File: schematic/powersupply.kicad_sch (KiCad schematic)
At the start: 15 parts

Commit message: Update schematic
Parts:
- added D13: 1N5908, Diode_THT:D_DO-201AE_P15.24mm_Horizontal, symbol Diode:1N5908
- C10: value 680 nF / 400 V -> 680 nF / 400 V= 250 V~
- C9: value 220 nF / 400 V -> 220 nF / 400 V= 250 V~
- R10, R11: value 100 / 0.5 W -> 100 / 2 W
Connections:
- net +5V: now also D13.1 (A1)
- net GND: now also D13.2 (A2)
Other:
- note added: "TVS"
- moved on the sheet: C10, C9, R10, R11, R12, R13, R14, R15

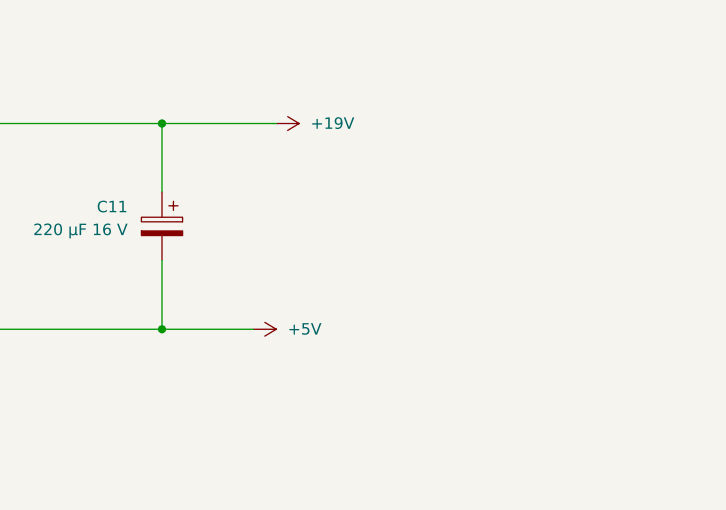
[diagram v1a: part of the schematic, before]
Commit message: schematic: Add TVS
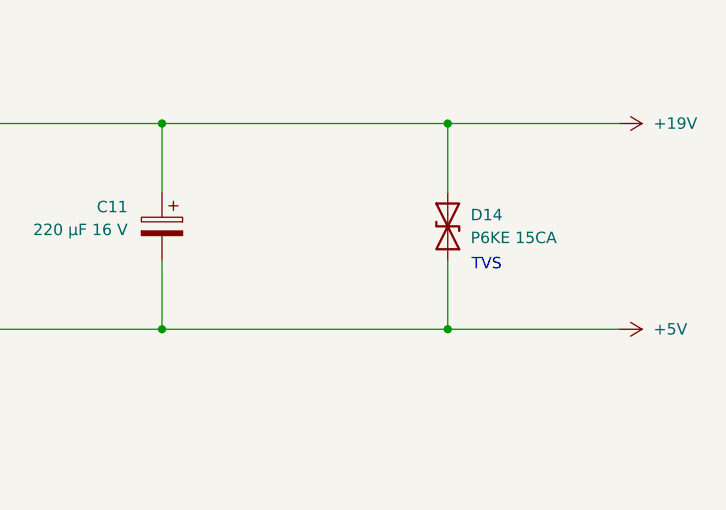
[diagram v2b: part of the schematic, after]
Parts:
- added D14: P6KE 15CA, Diode_THT:D_DO-201AE_P15.24mm_Horizontal, symbol Diode:1N62xxCA
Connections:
- net +19V: now also D14.2 (A2)
- net +5V: now also D14.1 (A1)
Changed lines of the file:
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@@
 		(company "Michael Büsch <m@bues.ch>")
+	)
+	(text "TVS"
+		(exclude_from_sim no)
+		(at 210.058 66.548 0)
+		(effects
+			(font
+				(size 1.27 1.27)
+			)
+		)
 	)
 	(text "+19 V rail"
@@
 	)
 	(junction
+		(at 205.74 50.8)
+		(diameter 0)
+		(color 0 0 0 0)
+	)
+	(junction
 		(at 180.34 115.57)
+		(diameter 0)
+		(color 0 0 0 0)
+	)
+	(junction
+		(at 205.74 73.66)
 		(diameter 0)
 		(color 0 0 0 0)
@@
 	(wire
 		(pts
+			(xy 205.74 66.04) (xy 205.74 73.66)
+		)
+		(stroke
+			(width 0)
+			(type default)
+		)
+	)
+	(wire
+		(pts
 			(xy 118.11 125.73) (xy 124.46 125.73)
 		)
@@
 	(wire
 		(pts
+			(xy 205.74 50.8) (xy 205.74 58.42)
+		)
+		(stroke
+			(width 0)
+			(type default)
+		)
+	)
+	(wire
+		(pts
 			(xy 147.32 71.12) (xy 147.32 73.66)
 		)
@@
 	(wire
 		(pts
-			(xy 173.99 73.66) (xy 184.15 73.66)
+			(xy 205.74 50.8) (xy 224.79 50.8)
+		)
+		(stroke
+			(width 0)
+			(type default)
+		)
+	)
+	(wire
+		(pts
+			(xy 173.99 73.66) (xy 205.74 73.66)
 		)
 		(stroke
@@
 	(wire
 		(pts
-			(xy 173.99 50.8) (xy 186.69 50.8)
+			(xy 173.99 50.8) (xy 205.74 50.8)
 		)
 		(stroke
@@
 		(pts
 			(xy 173.99 66.04) (xy 173.99 73.66)
+		)
+		(stroke
+			(width 0)
+			(type default)
+		)
+	)
+	(wire
+		(pts
+			(xy 205.74 73.66) (xy 224.79 73.66)
 		)
 		(stroke
@@
 	(symbol
 		(lib_id "power:+15V")
-		(at 186.69 50.8 270)
+		(at 224.79 50.8 270)
 		(unit 1)
 		(exclude_from_sim no)
@@
 		(fields_autoplaced yes)
 		(property "Reference" "#PWR016"
-			(at 182.88 50.8 0)
+			(at 220.98 50.8 0)
 			(effects
 				(font
@@
 		)
 		(property "Value" "+19V"
-			(at 190.5 50.7999 90)
+			(at 228.6 50.7999 90)
 			(effects
 				(font
@@
 		)
 		(property "Footprint" ""
-			(at 186.69 50.8 0)
+			(at 224.79 50.8 0)
 			(effects
 				(font
@@
 		)
 		(property "Datasheet" ""
-			(at 186.69 50.8 0)
+			(at 224.79 50.8 0)
 			(effects
 				(font
@@
 		)
 		(property "Description" "Power symbol creates a global label with name \"+15V\""
-			(at 186.69 50.8 0)
+			(at 224.79 50.8 0)
 			(effects
 				(font
@@
 	)
 	(symbol
+		(lib_id "Diode:1N62xxCA")
+		(at 205.74 62.23 90)
+		(unit 1)
+		(exclude_from_sim no)
+		(in_bom yes)
+		(on_board yes)
+		(dnp no)
+		(fields_autoplaced yes)
+		(property "Reference" "D14"
+			(at 208.28 60.9599 90)
+			(effects
+				(font
+					(size 1.27 1.27)
+				)
+				(justify right)
+			)
+		)
+		(property "Value" "P6KE 15CA"
+			(at 208.28 63.4999 90)
+			(effects
+				(font
+					(size 1.27 1.27)
+				)
+				(justify right)
+			)
+		)
+		(property "Footprint" "Diode_THT:D_DO-201AE_P15.24mm_Horizontal"
+			(at 210.82 62.23 0)
+			(effects
+				(font
+					(size 1.27 1.27)
+				)
+				(hide yes)
+			)
+		)
+		(property "Datasheet" "https://www.vishay.com/docs/88301/15ke.pdf"
+			(at 205.74 62.23 0)
+			(effects
+				(font
+					(size 1.27 1.27)
+				)
+				(hide yes)
+			)
+		)
+		(property "Description" "1500W bidirectional TRANSZORB® Transient Voltage Suppressor, DO-201AE"
+			(at 205.74 62.23 0)
+			(effects
+				(font
+					(size 1.27 1.27)
+				)
+				(hide yes)
+			)
+		)
+		(pin "1"
+		)
+		(pin "2"
+		)
+		(instances
+			(project "phaseanglecontrol"
+				(path "/167e0419-9f88-4ea4-ae96-d03af9cd26b8/bb8c6d96-af7e-4cb3-a868-b4a7ef100530"
+					(reference "D14")
+					(unit 1)
+				)
+			)
+		)
+	)
+	(symbol
 		(lib_id "Device:C_Polarized")
 		(at 173.99 125.73 0)
@@
 	(symbol
 		(lib_id "power:+5V")
-		(at 184.15 73.66 270)
+		(at 224.79 73.66 270)
 		(unit 1)
 		(exclude_from_sim no)
@@
 		(fields_autoplaced yes)
 		(property "Reference" "#PWR013"
-			(at 180.34 73.66 0)
+			(at 220.98 73.66 0)
 			(effects
 				(font
@@
 		)
 		(property "Value" "+5V"
-			(at 187.96 73.6599 90)
+			(at 228.6 73.6599 90)
 			(effects
 				(font
@@
 		)
 		(property "Footprint" ""
-			(at 184.15 73.66 0)
+			(at 224.79 73.66 0)
 			(effects
 				(font
@@
 		)
 		(property "Datasheet" ""
-			(at 184.15 73.66 0)
+			(at 224.79 73.66 0)
 			(effects
 				(font
@@
 		)
 		(property "Description" "Power symbol creates a global label with name \"+5V\""
-			(at 184.15 73.66 0)
-			(effects
-				(font
+			(at 224.79 73.66 0)
+			(effects
+				(font

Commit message: schematic: Add 2nd shutoff biasing
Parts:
- renumbered D13 to D10, D14 to D9, R10 to R11, R11 to R12, R12 to R13, R13 to R14, R14 to R15, R15 to R16
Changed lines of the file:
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@@
 		(dnp no)
 		(fields_autoplaced yes)
-		(property "Reference" "R14"
+		(property "Reference" "R15"
 			(at 133.35 64.77 90)
 			(effects
@@
 			(project "phaseanglecontrol"
 				(path "/167e0419-9f88-4ea4-ae96-d03af9cd26b8/bb8c6d96-af7e-4cb3-a868-b4a7ef100530"
-					(reference "R14")
+					(reference "R15")
 					(unit 1)
 				)
@@
 		(dnp no)
 		(fields_autoplaced yes)
-		(property "Reference" "R15"
+		(property "Reference" "R16"
 			(at 133.35 129.54 90)
 			(effects
@@
 			(project "phaseanglecontrol"
 				(path "/167e0419-9f88-4ea4-ae96-d03af9cd26b8/bb8c6d96-af7e-4cb3-a868-b4a7ef100530"
-					(reference "R15")
+					(reference "R16")
 					(unit 1)
 				)
@@
 		(dnp no)
 		(fields_autoplaced yes)
-		(property "Reference" "R12"
+		(property "Reference" "R13"
 			(at 123.19 64.77 90)
 			(effects
@@
 			(project "phaseanglecontrol"
 				(path "/167e0419-9f88-4ea4-ae96-d03af9cd26b8/bb8c6d96-af7e-4cb3-a868-b4a7ef100530"
-					(reference "R12")
+					(reference "R13")
 					(unit 1)
 				)
@@
 		(dnp no)
 		(fields_autoplaced yes)
-		(property "Reference" "R13"
+		(property "Reference" "R14"
 			(at 123.19 129.54 90)
 			(effects
@@
 			(project "phaseanglecontrol"
 				(path "/167e0419-9f88-4ea4-ae96-d03af9cd26b8/bb8c6d96-af7e-4cb3-a868-b4a7ef100530"
-					(reference "R13")
+					(reference "R14")
 					(unit 1)
 				)
@@
 		(on_board yes)
 		(dnp no)
-		(property "Reference" "R10"
+		(property "Reference" "R11"
 			(at 101.6 54.61 90)
 			(effects
@@
 			(project "phaseanglecontrol"
 				(path "/167e0419-9f88-4ea4-ae96-d03af9cd26b8/bb8c6d96-af7e-4cb3-a868-b4a7ef100530"
-					(reference "R10")
+					(reference "R11")
 					(unit 1)
 				)
@@
 		(dnp no)
 		(fields_autoplaced yes)
-		(property "Reference" "#PWR016"
+		(property "Reference" "#PWR014"
 			(at 220.98 50.8 0)
 			(effects
@@
 			(project "phaseanglecontrol"
 				(path "/167e0419-9f88-4ea4-ae96-d03af9cd26b8/bb8c6d96-af7e-4cb3-a868-b4a7ef100530"
-					(reference "#PWR016")
+					(reference "#PWR014")
 					(unit 1)
 				)
@@
 		(dnp no)
 		(fields_autoplaced yes)
-		(property "Reference" "#PWR014"
+		(property "Reference" "#PWR016"
 			(at 220.98 115.57 0)
 			(effects
@@
 			(project "phaseanglecontrol"
 				(path "/167e0419-9f88-4ea4-ae96-d03af9cd26b8/bb8c6d96-af7e-4cb3-a868-b4a7ef100530"
-					(reference "#PWR014")
+					(reference "#PWR016")
 					(unit 1)
 				)
@@
 		(dnp no)
 		(fields_autoplaced yes)
-		(property "Reference" "D14"
+		(property "Reference" "D9"
 			(at 208.28 60.9599 90)
 			(effects
@@
 			(project "phaseanglecontrol"
 				(path "/167e0419-9f88-4ea4-ae96-d03af9cd26b8/bb8c6d96-af7e-4cb3-a868-b4a7ef100530"
-					(reference "D14")
+					(reference "D9")
 					(unit 1)
 				)
@@
 		(dnp no)
 		(fields_autoplaced yes)
-		(property "Reference" "D13"
+		(property "Reference" "D10"
 			(at 208.28 124.4599 90)
 			(effects
@@
 			(project ""
 				(path "/167e0419-9f88-4ea4-ae96-d03af9cd26b8/bb8c6d96-af7e-4cb3-a868-b4a7ef100530"
-					(reference "D13")
+					(reference "D10")
 					(unit 1)
 				)
@@
 		(on_board yes)
 		(dnp no)
-		(property "Reference" "R11"
+		(property "Reference" "R12"
 			(at 101.6 119.38 90)
 			(effects
@@
 			(project "phaseanglecontrol"
 				(path "/167e0419-9f88-4ea4-ae96-d03af9cd26b8/bb8c6d96-af7e-4cb3-a868-b4a7ef100530"
-					(reference "R11")
+					(reference "R12")
 					(unit 1)
 				)
@@
 		(dnp no)
 		(fields_autoplaced yes)
-		(property "Reference" "#PWR015"
+		(property "Reference" "#PWR017"
 			(at 232.41 135.89 0)
 			(effects
@@
 			(project "phaseanglecontrol"
 				(path "/167e0419-9f88-4ea4-ae96-d03af9cd26b8/bb8c6d96-af7e-4cb3-a868-b4a7ef100530"
-					(reference "#PWR015")
+					(reference "#PWR017")
 					(unit 1)
 				)
@@
 		(dnp no)
 		(fields_autoplaced yes)
-		(property "Reference" "#PWR013"
+		(property "Reference" "#PWR015"
 			(at 220.98 73.66 0)
 			(effects
@@
 			(project "phaseanglecontrol"
 				(path "/167e0419-9f88-4ea4-ae96-d03af9cd26b8/bb8c6d96-af7e-4cb3-a868-b4a7ef100530"
-					(reference "#PWR013")
-					(unit 1)
-				)
+					(reference "#PWR015")
+					(unit 1)
+				)

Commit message: Add TVS to tirac gate
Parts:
- renumbered D9 to D10, D10 to D11, D5 to D6, D6 to D7, D7 to D8, D8 to D9
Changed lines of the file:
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@@
 		(dnp no)
 		(fields_autoplaced yes)
-		(property "Reference" "#PWR014"
+		(property "Reference" "#PWR015"
 			(at 220.98 50.8 0)
 			(effects
@@
 			(project "phaseanglecontrol"
 				(path "/167e0419-9f88-4ea4-ae96-d03af9cd26b8/bb8c6d96-af7e-4cb3-a868-b4a7ef100530"
-					(reference "#PWR014")
+					(reference "#PWR015")
 					(unit 1)
 				)
@@
 		(dnp no)
 		(fields_autoplaced yes)
-		(property "Reference" "#PWR016"
+		(property "Reference" "#PWR017"
 			(at 220.98 115.57 0)
 			(effects
@@
 			(project "phaseanglecontrol"
 				(path "/167e0419-9f88-4ea4-ae96-d03af9cd26b8/bb8c6d96-af7e-4cb3-a868-b4a7ef100530"
-					(reference "#PWR016")
+					(reference "#PWR017")
 					(unit 1)
 				)
@@
 		(dnp no)
 		(fields_autoplaced yes)
-		(property "Reference" "D9"
+		(property "Reference" "D10"
 			(at 208.28 60.9599 90)
 			(effects
@@
 			(project "phaseanglecontrol"
 				(path "/167e0419-9f88-4ea4-ae96-d03af9cd26b8/bb8c6d96-af7e-4cb3-a868-b4a7ef100530"
-					(reference "D9")
+					(reference "D10")
 					(unit 1)
 				)
@@
 		(dnp no)
 		(fields_autoplaced yes)
-		(property "Reference" "D10"
+		(property "Reference" "D11"
 			(at 208.28 124.4599 90)
 			(effects
@@
 			(project ""
 				(path "/167e0419-9f88-4ea4-ae96-d03af9cd26b8/bb8c6d96-af7e-4cb3-a868-b4a7ef100530"
-					(reference "D10")
+					(reference "D11")
 					(unit 1)
 				)
@@
 		(dnp no)
 		(fields_autoplaced yes)
-		(property "Reference" "D7"
+		(property "Reference" "D8"
 			(at 149.86 119.3799 90)
 			(effects
@@
 			(project "phaseanglecontrol"
 				(path "/167e0419-9f88-4ea4-ae96-d03af9cd26b8/bb8c6d96-af7e-4cb3-a868-b4a7ef100530"
-					(reference "D7")
+					(reference "D8")
 					(unit 1)
 				)
@@
 		(dnp no)
 		(fields_autoplaced yes)
-		(property "Reference" "#PWR017"
+		(property "Reference" "#PWR018"
 			(at 232.41 135.89 0)
 			(effects
@@
 			(project "phaseanglecontrol"
 				(path "/167e0419-9f88-4ea4-ae96-d03af9cd26b8/bb8c6d96-af7e-4cb3-a868-b4a7ef100530"
-					(reference "#PWR017")
+					(reference "#PWR018")
 					(unit 1)
 				)
@@
 		(dnp no)
 		(fields_autoplaced yes)
-		(property "Reference" "#PWR015"
+		(property "Reference" "#PWR016"
 			(at 220.98 73.66 0)
 			(effects
@@
 			(project "phaseanglecontrol"
 				(path "/167e0419-9f88-4ea4-ae96-d03af9cd26b8/bb8c6d96-af7e-4cb3-a868-b4a7ef100530"
-					(reference "#PWR015")
+					(reference "#PWR016")
 					(unit 1)
 				)
@@
 		(dnp no)
 		(fields_autoplaced yes)
-		(property "Reference" "D8"
+		(property "Reference" "D9"
 			(at 149.86 129.5399 90)
 			(effects
@@
 			(project "phaseanglecontrol"
 				(path "/167e0419-9f88-4ea4-ae96-d03af9cd26b8/bb8c6d96-af7e-4cb3-a868-b4a7ef100530"
-					(reference "D8")
+					(reference "D9")
 					(unit 1)
 				)
@@
 		(dnp no)
 		(fields_autoplaced yes)
-		(property "Reference" "D5"
+		(property "Reference" "D6"
 			(at 149.86 54.6099 90)
 			(effects
@@
 			(project "phaseanglecontrol"
 				(path "/167e0419-9f88-4ea4-ae96-d03af9cd26b8/bb8c6d96-af7e-4cb3-a868-b4a7ef100530"
-					(reference "D5")
+					(reference "D6")
 					(unit 1)
 				)
@@
 		(dnp no)
 		(fields_autoplaced yes)
-		(property "Reference" "D6"
+		(property "Reference" "D7"
 			(at 149.86 66.0399 90)
 			(effects
@@
 			(project "phaseanglecontrol"
 				(path "/167e0419-9f88-4ea4-ae96-d03af9cd26b8/bb8c6d96-af7e-4cb3-a868-b4a7ef100530"
-					(reference "D6")
-					(unit 1)
-				)
+					(reference "D7")
+					(unit 1)
+				)

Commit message: schematic: Minor cleanups
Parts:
- D10: footprint Diode_THT:D_DO-201AE_P15.24mm_Horizontal -> (none)
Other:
- note removed: "TVS"
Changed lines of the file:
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@@
 		(company "Michael Büsch <m@bues.ch>")
-	)
-	(text "TVS"
-		(exclude_from_sim no)
-		(at 210.058 66.548 0)
-		(effects
-			(font
-				(size 1.27 1.27)
-			)
-		)
 	)
 	(text "+19 V rail"
@@
 		(exclude_from_sim no)
 		(at 146.05 107.442 0)
-		(effects
-			(font
-				(size 1.27 1.27)
-			)
-		)
-	)
-	(text "TVS"
-		(exclude_from_sim no)
-		(at 210.058 129.794 0)
 		(effects
 			(font
@@
 		(on_board yes)
 		(dnp no)
-		(fields_autoplaced yes)
 		(property "Reference" "D10"
 			(at 208.28 60.9599 90)
@@
 			)
 		)
-		(property "Footprint" "Diode_THT:D_DO-201AE_P15.24mm_Horizontal"
+		(property "Footprint" ""
 			(at 210.82 62.23 0)
 			(effects
@@
 			)
 		)
-		(property "Datasheet" "https://www.vishay.com/docs/88301/15ke.pdf"
+		(property "Datasheet" ""
 			(at 205.74 62.23 0)
 			(effects
@@
 			)
 		)
-		(property "Description" "1500W bidirectional TRANSZORB® Transient Voltage Suppressor, DO-201AE"
-			(at 205.74 62.23 0)
-			(effects
-				(font
-					(size 1.27 1.27)
-				)
-				(hide yes)
+		(property "Description" "TVS"
+			(at 210.058 66.04 90)
+			(effects
+				(font
+					(size 1.27 1.27)
+				)
 			)
 		)
@@
 		(on_board yes)
 		(dnp no)
-		(fields_autoplaced yes)
 		(property "Reference" "D11"
 			(at 208.28 124.4599 90)
@@
 			)
 		)
-		(property "Description" "1500W (10/1000 μs) Unidirectional TVS Diode, VRM = 5V (IRM = 300 μA at 25°C), VBR = 6V, DO-201AE"
-			(at 199.136 125.73 0)
-			(effects
-				(font
-					(size 1.27 1.27)
-				)
-				(hide yes)
-			)
-		)
+		(property "Description" "TVS"
+			(at 210.312 129.54 90)
+			(effects
+				(font
+					(size 1.27 1.27)
+				)
+			)
+		)
